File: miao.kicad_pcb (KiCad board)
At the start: 2 copper layers, 17.8 x 21 mm, 17 parts, among them J1 USB_C_Receptacle_USB2.0, U2 USBLC6-2SC6, U3 xiao_drop-in_gpio_usb_no_cuto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

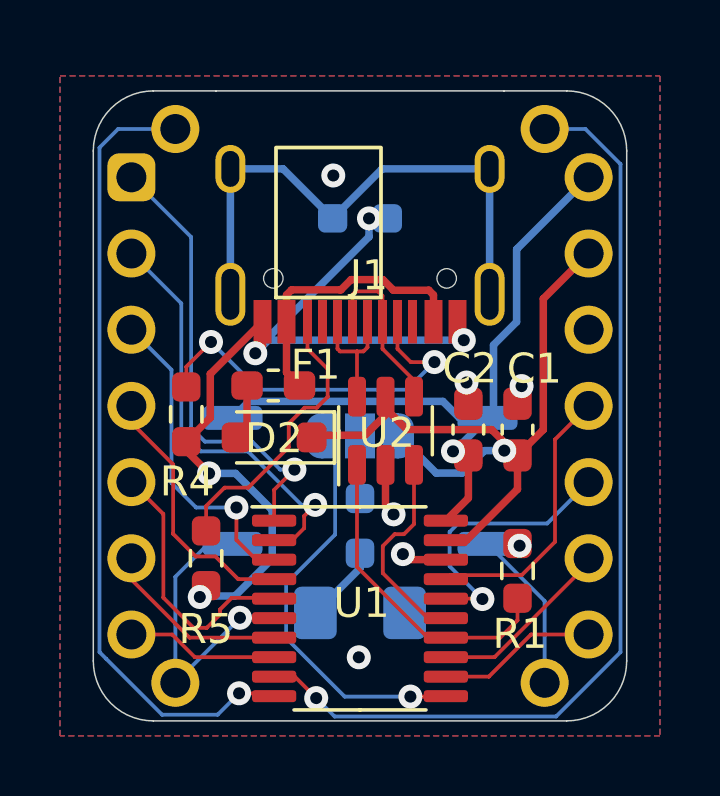
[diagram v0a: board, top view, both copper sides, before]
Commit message: hopefully fix pin-out errors to add more compat
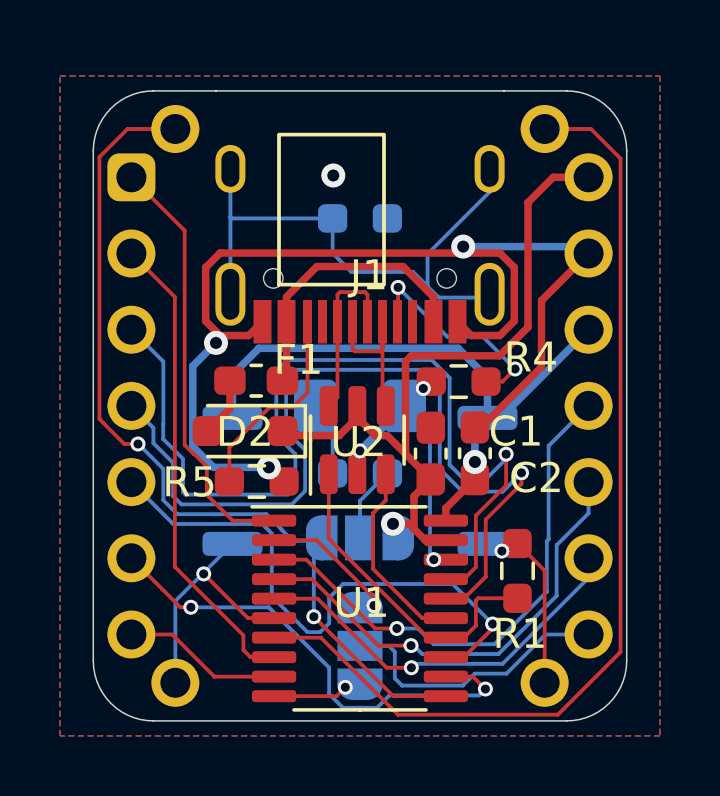
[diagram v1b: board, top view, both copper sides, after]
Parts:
- added JP2: SolderJumper_3_Open, BeiBob:SolderJumper-3_P1.3mm_Open_RoundedPad1.0x1.5mm_NumberLabels, B.Cu at (149.0, 113.0)
- D2: value PMEG2010BELD -> PMEG2010EA
- moved R4 9.15 mm to (152.3, 104.2), turned to 180 degrees
- moved D1 6.90 mm to (149.0, 105.0)
- moved JP1 3.40 mm to (149.0, 109.4)
- moved R5 3.07 mm to (145.6, 107.5), turned to 0 degrees
- moved C1 3.00 mm to (151.4, 106.6)
- moved R2 1.75 mm to (149.0, 107.2), turned to 180 degrees
- moved D2 0.99 mm to (145.2, 105.8)
- moved U2 0.99 mm to (148.9, 106.1)
- moved C2 0.82 mm to (152.8, 106.6)
- moved F1 0.59 mm to (145.5, 104.2)
- renumbered LED to D1
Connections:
- net P3.2 renamed P3.2_A3
- U1 pad 10: P3.0 -> P3.0_RX
- U1 pad 2: P1.4 -> P1.4_CS
- U1 pad 3: P1.5 -> P1.5_MOSI
- U1 pad 4: P1.6 -> P1.6_MISO
- U1 pad 5: P1.7 -> P1.7_SCK
- U1 pad 8: P1.1 -> P1.1_A0
- U1 pad 9: P3.1 -> P3.1_TX
- U3 pad 10: P1.3 -> P1.6_MISO
- U3 pad 11: P1.2 -> P1.5_MOSI
- U3 pad 12: GND -> +3.3V
- U3 pad 13: VCC -> GND
- U3 pad 14: +3.3V -> VCC
- U3 pad 17: P3.1 -> P1.0
- U3 pad 18: P3.0 -> P3.3
- U3 pad 2: P1.4 -> P1.1_A0
- U3 pad 3: P1.5 -> P1.2
- U3 pad 4: P1.6 -> P1.3
- U3 pad 5: P1.7 -> P3.5
- U3 pad 6: P1.0 -> P3.4
- U3 pad 7: P1.1 -> P3.1_TX
- U3 pad 8: P3.4 -> RX/CS
- U3 pad 9: P3.5 -> P1.7_SCK
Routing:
- net P3.1: track 32.3 -> 0.00 mm, vias 1 -> 0
- net P3.0: track 26.6 -> 0.00 mm, vias 1 -> 0
- net P1.0: track 6.27 -> 32.9 mm
- net P1.2: track 9.15 -> 31.2 mm, vias 0 -> 1
- net P1.3: track 9.23 -> 29.6 mm
- net P1.5_MOSI: track 0.00 -> 17.8 mm, vias 0 -> 1
- net P1.1_A0: track 0.00 -> 15.9 mm
- net P3.3: track 13.7 -> 29.3 mm, vias 1 -> 2
- net GND: track 31.7 -> 47.2 mm, vias 11 -> 7
- net P1.6_MISO: track 0.00 -> 15.5 mm, vias 0 -> 1
- net P1.4: track 14.2 -> 0.00 mm, vias 1 -> 0
- net P1.7_SCK: track 0.00 -> 13.3 mm, vias 0 -> 1
- net P3.5: track 6.22 -> 19.2 mm, vias 0 -> 1
- net P3.4: track 5.34 -> 16.1 mm, vias 0 -> 2
- net P1.5: track 10.8 -> 0.00 mm, vias 1 -> 0
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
